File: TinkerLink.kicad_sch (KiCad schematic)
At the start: 26 parts, among them J1 Conn_01x06_Pin, Q2 MMBT2222A, Q3 SQS411ENW-T1_GE3, Q4 SQS411ENW-T1_GE3, SW1 TS-061D-250D4-P, U1 ESP-01F-2M, U16 INA228, U3 AP63203WU, U5 TPD2EUSB30A

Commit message: ...
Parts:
- renumbered C86 to C1, R47 to R1, R1 to R2, R2 to R4, U16 to U2, U5 to U4
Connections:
- net Vbus: no longer C5.1, Q3.1 (S), Q3.2 (S), Q3.3 (S), R1.1, R2.1, U2.9 (Vin-), U3.2 (EN), U3.3 (IN)
- net Ant10a: now reaches U1.1 (ANT)
- new net VbusX: C5.1, Q3.1 (S), Q3.2 (S), Q3.3 (S), R1.1, R2.1, U2.9 (Vin-), U3.2 (EN), U3.3 (IN)
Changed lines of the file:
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@@
 	(wire
 		(pts
+			(xy 139.7 109.22) (xy 142.24 109.22)
+		)
+		(stroke
+			(width 0)
+			(type default)
+		)
+	)
+	(wire
+		(pts
 			(xy 220.98 102.87) (xy 224.79 102.87)
 		)
@@
 	(wire
 		(pts
-			(xy 101.6 55.88) (xy 93.98 55.88)
-		)
-		(stroke
-			(width 0)
-			(type default)
-		)
-	)
-	(wire
-		(pts
 			(xy 168.91 58.42) (xy 168.91 60.96)
 		)
@@
 	(wire
 		(pts
+			(xy 142.24 109.22) (xy 142.24 120.65)
+		)
+		(stroke
+			(width 0)
+			(type default)
+		)
+	)
+	(wire
+		(pts
 			(xy 172.72 123.19) (xy 172.72 113.03)
 		)
@@
 		)
 	)
+	(global_label "Ant10a"
+		(shape input)
+		(at 139.7 109.22 180)
+		(fields_autoplaced yes)
+		(effects
+			(font
+				(size 1.27 1.27)
+			)
+			(justify right)
+		)
+		(property "Intersheetrefs" "${INTERSHEET_REFS}"
+			(at 130.1835 109.22 0)
+			(effects
+				(font
+					(size 1.27 1.27)
+				)
+				(justify right)
+				(hide yes)
+			)
+		)
+	)
 	(global_label "io16"
 		(shape input)
@@
 		(on_board yes)
 		(dnp no)
-		(property "Reference" "R47"
+		(property "Reference" "R1"
 			(at 94.488 50.292 90)
 			(effects
@@
 			(project "TinkerLink"
 				(path "/d9db63b9-0e33-4ffc-b3bb-ae5011fef151"
-					(reference "R47")
+					(reference "R1")
 					(unit 1)
 				)
@@
 		(on_board yes)
 		(dnp no)
-		(property "Reference" "R1"
+		(property "Reference" "R2"
 			(at 128.3716 61.722 0)
 			(effects
@@
 			(project "TinkerLink"
 				(path "/d9db63b9-0e33-4ffc-b3bb-ae5011fef151"
-					(reference "R1")
+					(reference "R2")
 					(unit 1)
 				)
@@
 		(on_board yes)
 		(dnp no)
-		(property "Reference" "U16"
+		(property "Reference" "U2"
 			(at 104.902 66.802 90)
 			(effects
@@
 			(project "TinkerLink"
 				(path "/d9db63b9-0e33-4ffc-b3bb-ae5011fef151"
-					(reference "U16")
+					(reference "U2")
 					(unit 1)
 				)
@@
 		(on_board yes)
 		(dnp no)
-		(property "Reference" "U5"
+		(property "Reference" "U4"
 			(at 38.1 77.4699 90)
 			(effects
@@
 			(project "TinkerLink"
 				(path "/d9db63b9-0e33-4ffc-b3bb-ae5011fef151"
-					(reference "U5")
+					(reference "U4")
 					(unit 1)
 				)
@@
 		(on_board yes)
 		(dnp no)
-		(property "Reference" "R2"
+		(property "Reference" "R4"
 			(at 149.7584 80.518 0)
 			(effects
@@
 			(project "TinkerLink"
 				(path "/d9db63b9-0e33-4ffc-b3bb-ae5011fef151"
-					(reference "R2")
+					(reference "R4")
 					(unit 1)
 				)
@@
 		(on_board yes)
 		(dnp no)
-		(property "Reference" "C86"
+		(property "Reference" "C1"
 			(at 73.66 80.01 0)
 			(effects
@@
 			(project "TinkerLink"
 				(path "/d9db63b9-0e33-4ffc-b3bb-ae5011fef151"
-					(reference "C86")
+					(reference "C1")
 					(unit 1)
 				)

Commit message: BOM, Notes, ...
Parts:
- C1: LCSC C14663 -> (none); LCSC Part (none) -> C14663
- C7, C8: LCSC Part (none) -> C20416425
- J1, LOGO1: now left out of the parts list
- R1: LCSC C710257 -> (none); LCSC Part (none) -> C710257
- U2: LCSC C2887910 -> (none); LCSC Part (none) -> C2887910
- U3: LCSC Part (none) -> C780769
- USB1: LCSC Part2 (none) -> C2765186
- USB2: LCSC Part C5370430, C2765186 -> C5370430; LCSC Part2 (none) -> C2765186

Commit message: smaller AC logo
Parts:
- LOGO1: value Creations_logo_med -> Creations_logo_small; footprint AUSTINfootprints:Creations logo med -> AC_logos:Creations logo small; symbol AC_logos:Creations_logo_med -> AC_logos:Creations_logo_small; now in the parts list
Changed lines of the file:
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@@
 	)
 	(symbol
-		(lib_id "AC_logos:Creations_logo_med")
+		(lib_id "AC_logos:Creations_logo_small")
 		(at 19.05 24.13 0)
 		(unit 1)
 		(exclude_from_sim no)
-		(in_bom no)
+		(in_bom yes)
 		(on_board yes)
 		(dnp no)
@@
 			)
 		)
-		(property "Value" "Creations_logo_med"
+		(property "Value" "Creations_logo_small"
 			(at 21.59 25.6539 0)
 			(effects
@@
 			)
 		)
-		(property "Footprint" "AUSTINfootprints:Creations logo med"
+		(property "Footprint" "AC_logos:Creations logo small"
 			(at 35.814 27.686 0)
 			(effects

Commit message: Nasty initial CC1/2 resistors solution
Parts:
- added R7, R8: 5k1, Resistor_SMD:R_0603_1608Metric, symbol Device:R
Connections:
- net GND: now also R7.2, R8.2
- net CC renamed CC1
- net CC1: now also R8.1
- net Vconn renamed CC2
- net CC2: now also R7.1
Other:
- note added: "So... How about swapping in an INA226, INA237, INAwhatever..."

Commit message: workin on some included libs...
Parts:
- LOGO1: footprint AC_logos:Creations logo small -> AUSTINfootprints:Creations logo small
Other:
- note added: "Button"
- note added: "I2C"
- note added: "LED"
- note added: "Vbus control"
- note removed: "LedLink"
- note removed: "Led_i 1"
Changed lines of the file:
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@@
 		)
 	)
-	(text "Led_i 1"
+	(text "tinker:USB-A-USB-C"
 		(exclude_from_sim no)
-		(at 108.712 136.652 0)
+		(at 43.434 59.436 0)
 		(effects
 			(font
@@
 		)
 	)
-	(text "LedLink"
+	(text "Button"
 		(exclude_from_sim no)
-		(at 108.204 126.238 0)
+		(at 113.284 138.43 0)
 		(effects
 			(font
@@
 		)
 	)
-	(text "tinker:USB-A-USB-C"
+	(text "LED"
 		(exclude_from_sim no)
-		(at 43.434 59.436 0)
+		(at 114.3 133.604 0)
 		(effects
 			(font
@@
 		)
 	)
+	(text "I2C"
+		(exclude_from_sim no)
+		(at 207.264 134.874 0)
+		(effects
+			(font
+				(size 1.27 1.27)
+			)
+		)
+	)
+	(text "Vbus control"
+		(exclude_from_sim no)
+		(at 110.49 135.89 0)
+		(effects
+			(font
+				(size 1.27 1.27)
+			)
+		)
+	)
 	(junction
 		(at 137.16 63.5)
@@
 			)
 		)
-		(property "Footprint" "AC_logos:Creations logo small"
+		(property "Footprint" "AUSTINfootprints:Creations logo small"
 			(at 35.814 27.686 0)
 			(effects

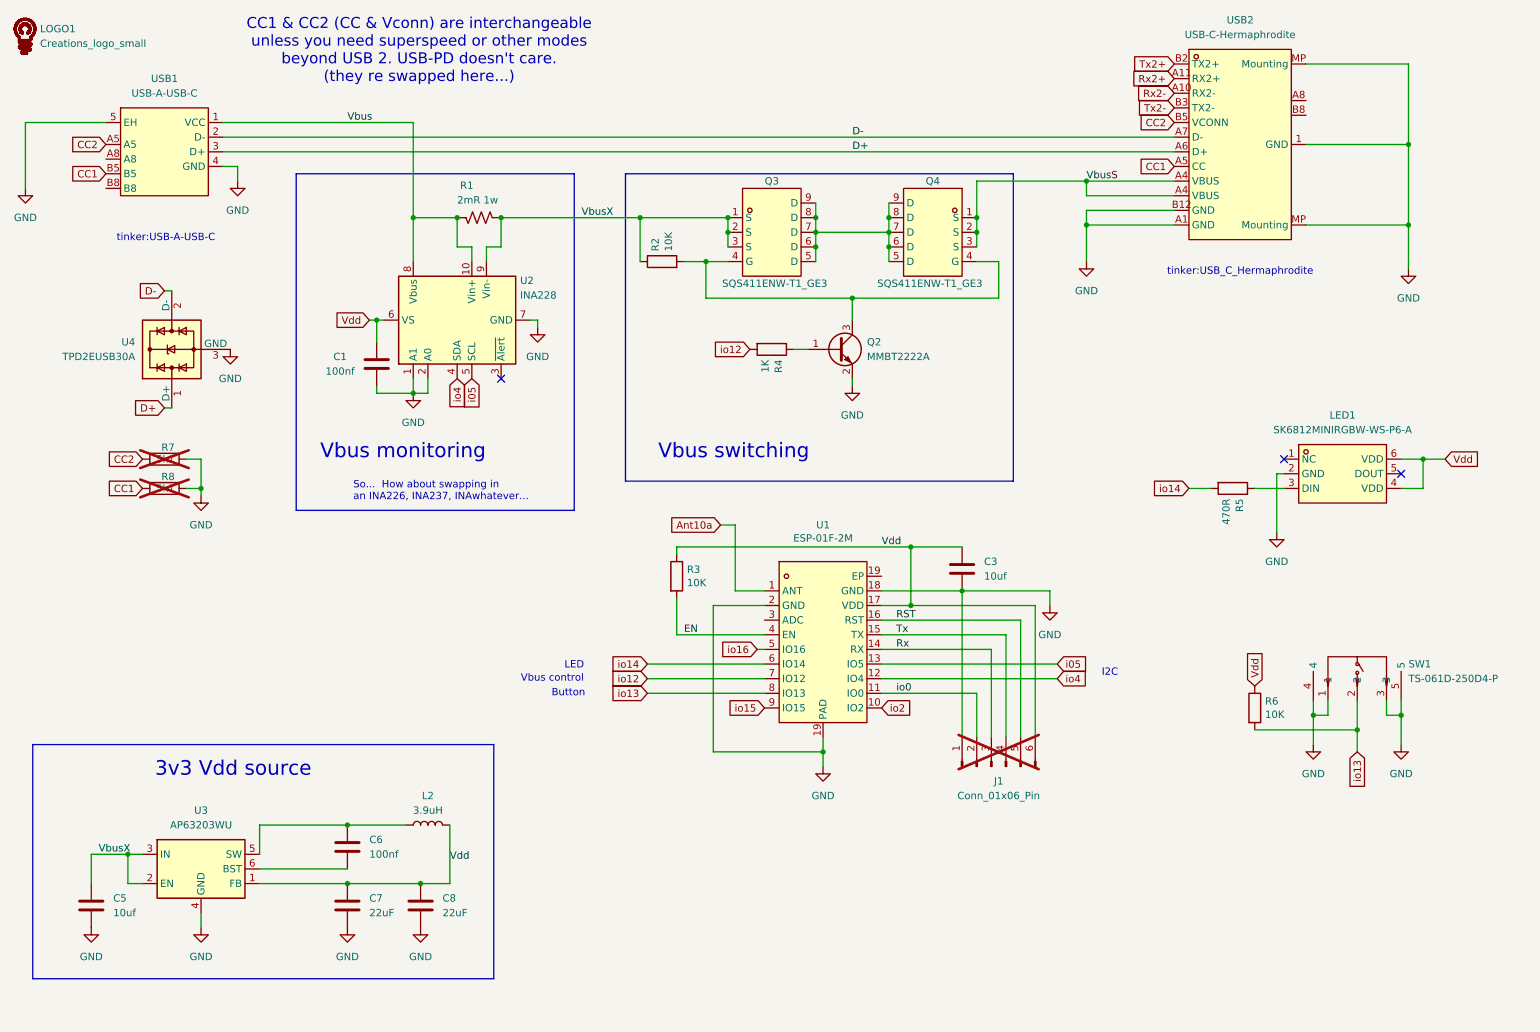
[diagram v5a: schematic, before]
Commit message: CC1&2 resistors now controllable
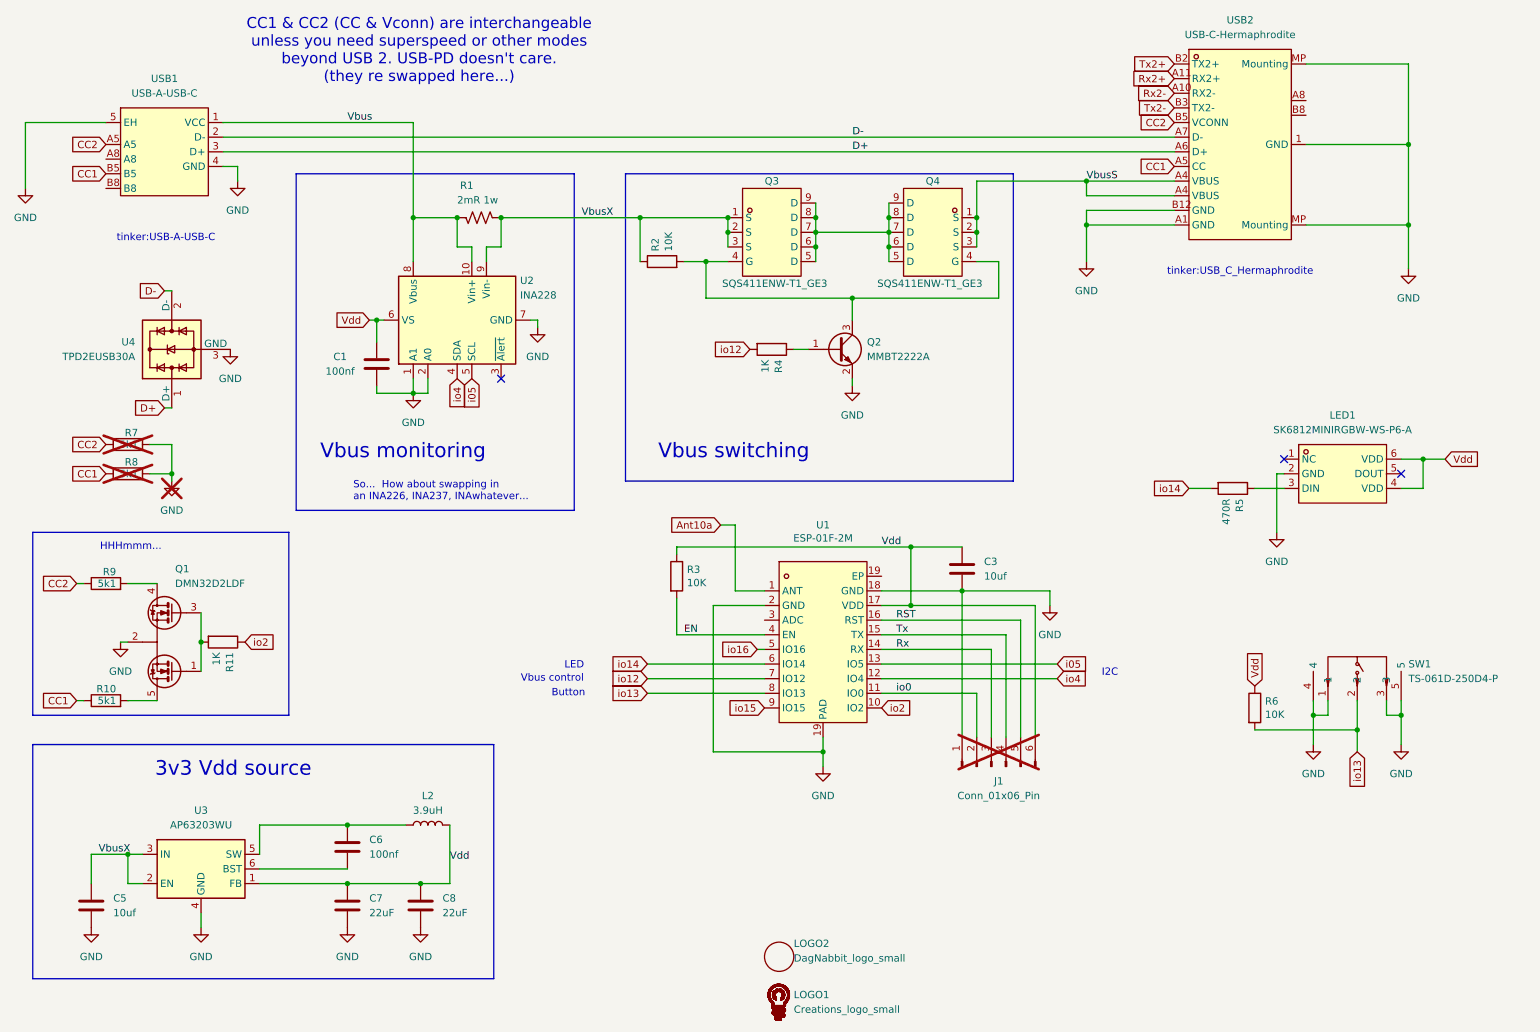
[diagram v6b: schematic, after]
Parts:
- added LOGO2: DagNabbit_logo_small, TINKERfootprints:DagNabbit, symbol TINKERLibrary:Tinker_logo_small
- added Q1: DMN32D2LDF, Package_TO_SOT_SMD:SOT-353_SC-70-5, symbol Transistor_FET:DMN32D2LDF
- added R10, R9: 5k1, Resistor_SMD:R_0603_1608Metric, symbol Device:R
- added R11: 1K, Resistor_SMD:R_0603_1608Metric, symbol Device:R
- LOGO1: symbol AC_logos:Creations_logo_small -> AUSTINLibrary:Creations_logo_small
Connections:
- net CC1: now also R10.1
- net CC2: now also R9.1
- net GND: now also Q1.2 (S)
- net io2: now also R11.1
- new net: Q1.1 (G1), Q1.3 (G2), R11.2
- new net: Q1.4 (D2), R9.2
- new net: Q1.5 (D1), R10.2
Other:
- note added: "HHHmmm..."
- moved on the sheet: LOGO1, R7, R8

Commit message: i THINK I have the repo libs workin'
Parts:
- J1: symbol Connector:Conn_01x06_Pin -> TINKERLibrary:Conn_01x06_Pin; now in the parts list
- USB1: symbol Tinker_Lib:USB-A-USB-C -> TINKERLibrary:USB-A-USB-C
- USB2: symbol Tinker_Lib:USB-C-Hermaphrodite -> TINKERLibrary:USB-C-Hermaphrodite; LCSC Part C5370430 -> C5370430, C2765186
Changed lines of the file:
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@@
 	)
 	(symbol
-		(lib_id "Tinker_Lib:USB-C-Hermaphrodite")
+		(lib_id "TINKERLibrary:USB-C-Hermaphrodite")
 		(at 228.6 43.18 0)
 		(unit 1)
@@
 			)
 		)
-		(property "LCSC Part" "C5370430"
+		(property "LCSC Part" "C5370430,  C2765186"
 			(at 228.6 74.93 0)
 			(effects
@@
 	)
 	(symbol
-		(lib_id "Tinker_Lib:USB-A-USB-C")
+		(lib_id "TINKERLibrary:USB-A-USB-C")
 		(at 43.18 43.18 0)
 		(unit 1)
@@
 	)
 	(symbol
-		(lib_id "Connector:Conn_01x06_Pin")
+		(lib_id "TINKERLibrary:Conn_01x06_Pin")
 		(at 186.69 151.13 90)
 		(unit 1)
 		(exclude_from_sim no)
-		(in_bom no)
+		(in_bom yes)
 		(on_board yes)
 		(dnp yes)

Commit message: ...
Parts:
- J1: footprint tinker:ProgHeader_1x06_P2.00mm -> TINKERfootprints:ProgHeader_1x06_P2.00mm
- USB1: footprint tinker:USB-A-USB-C -> TINKERfootprints:USB-A-USB-C
- USB2: footprint tinker:USB_C_Hermaphrodite -> TINKERfootprints:USB_C_Hermaphrodite
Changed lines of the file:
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@@
 			)
 		)
-		(property "Footprint" "tinker:USB_C_Hermaphrodite"
+		(property "Footprint" "TINKERfootprints:USB_C_Hermaphrodite"
 			(at 228.6 64.77 0)
 			(effects
@@
 			)
 		)
-		(property "Footprint" "tinker:USB-A-USB-C"
+		(property "Footprint" "TINKERfootprints:USB-A-USB-C"
 			(at 43.18 54.61 0)
 			(effects
@@
 			)
 		)
-		(property "Footprint" "tinker:ProgHeader_1x06_P2.00mm"
+		(property "Footprint" "TINKERfootprints:ProgHeader_1x06_P2.00mm"
 			(at 186.69 151.13 0)
 			(effects
